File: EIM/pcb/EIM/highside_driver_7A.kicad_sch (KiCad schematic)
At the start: 6 parts, among them Q2 BSS138, U7 BTS6142D

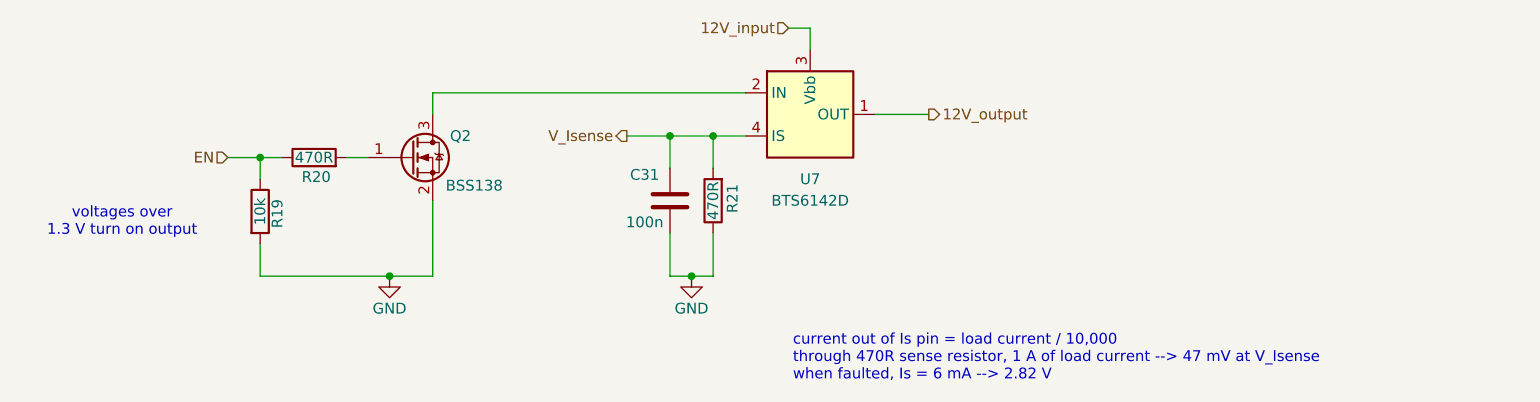
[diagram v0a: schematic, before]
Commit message: added Arjun's comments, assigned some MCU pins
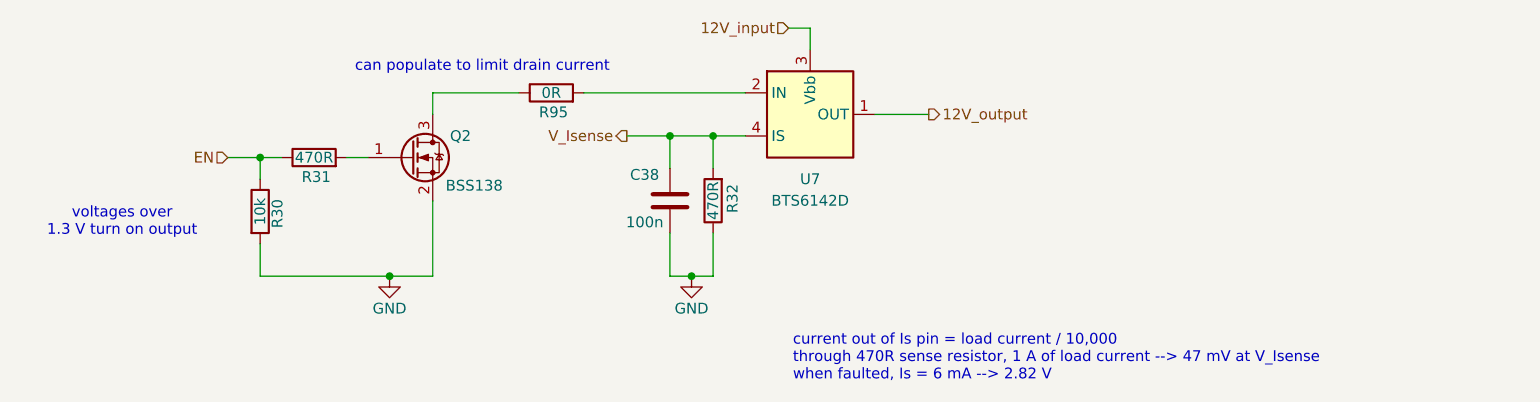
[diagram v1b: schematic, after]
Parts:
- added R95: 0R, Resistor_SMD:R_0805_2012Metric_Pad1.20x1.40mm_HandSolder, symbol Device:R
- renumbered C31 to C38, R19 to R30, R20 to R31, R21 to R32
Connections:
- net at Q2.3 (D): now also R95.1; no longer U7.2 (IN)
- new net: R95.2, U7.2 (IN)
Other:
- note added: "can populate to limit drain current"

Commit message: Layout 75% done, before 8V bus deletion
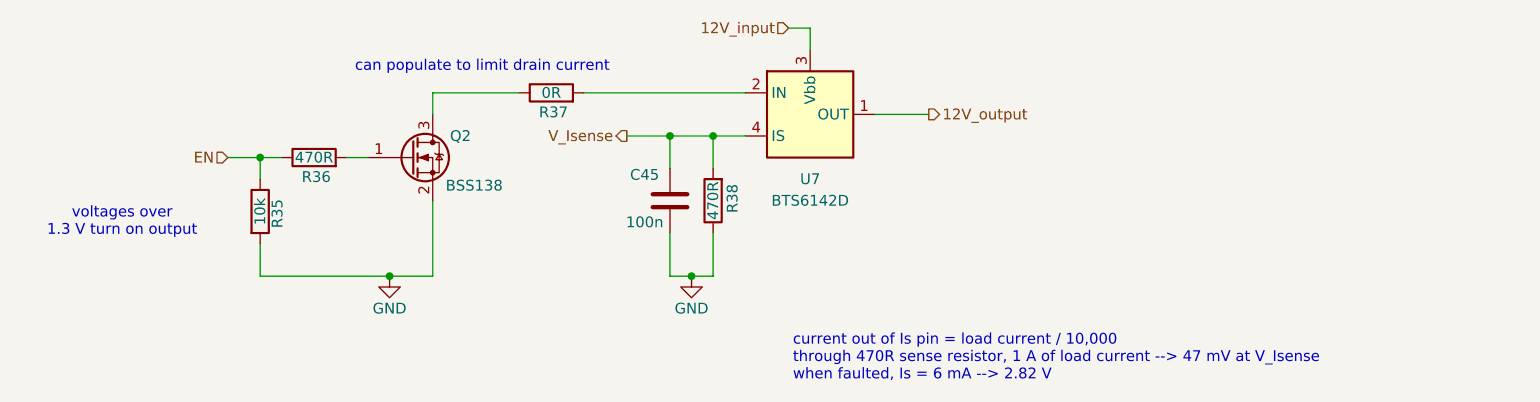
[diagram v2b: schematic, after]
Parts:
- renumbered C38 to C45, R30 to R35, R31 to R36, R95 to R37, R32 to R38

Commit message: All components placed and pins assigned.
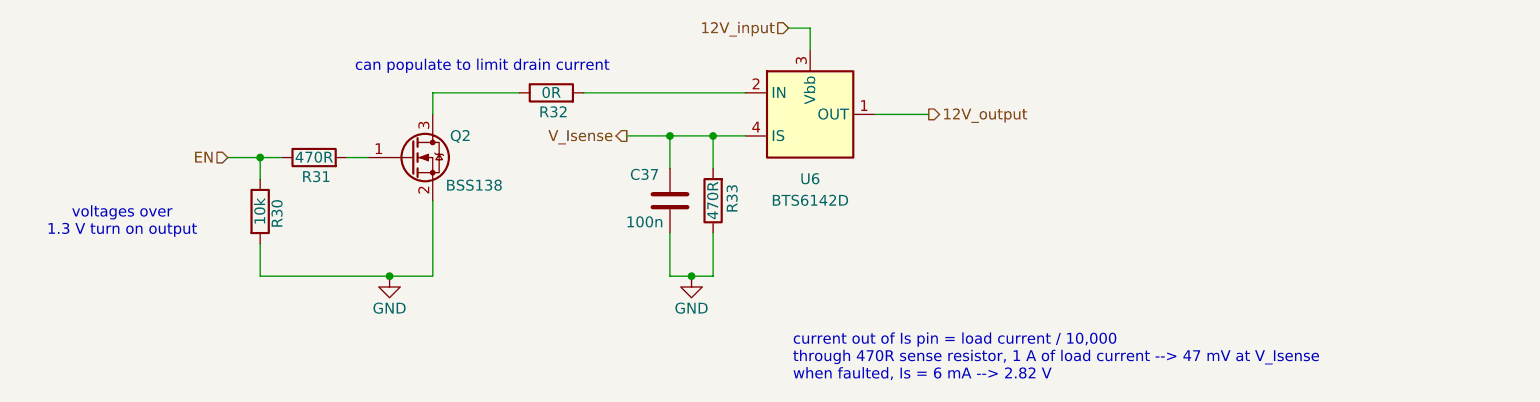
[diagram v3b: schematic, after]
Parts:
- renumbered C45 to C37, R35 to R30, R36 to R31, R37 to R32, R38 to R33, U7 to U6
